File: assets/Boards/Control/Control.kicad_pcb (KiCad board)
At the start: 2 copper layers, 59.7 x 22.9 mm, 7 parts, among them J3 MAIN_BOARD, J5 MIC, SW1 SW_Push_Dual

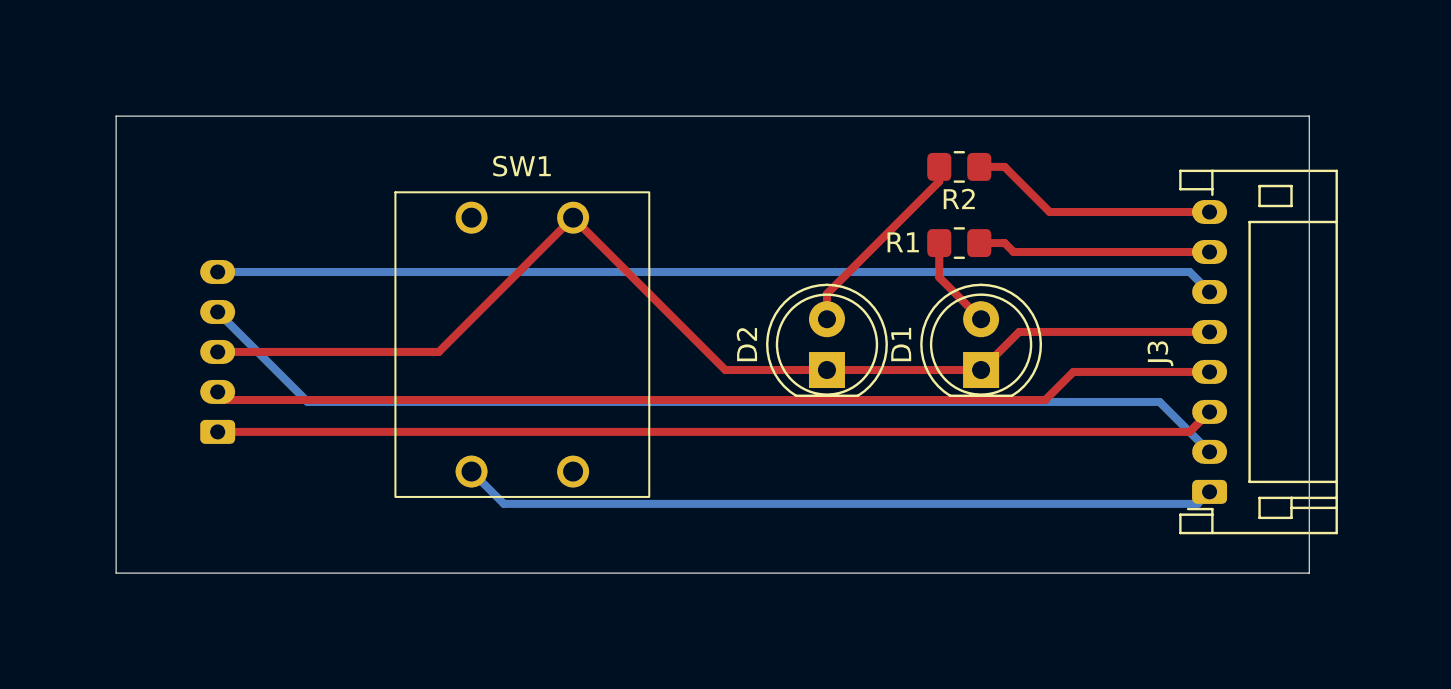
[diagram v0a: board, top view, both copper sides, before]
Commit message: Added ground plane, RF shield soldering points and text.
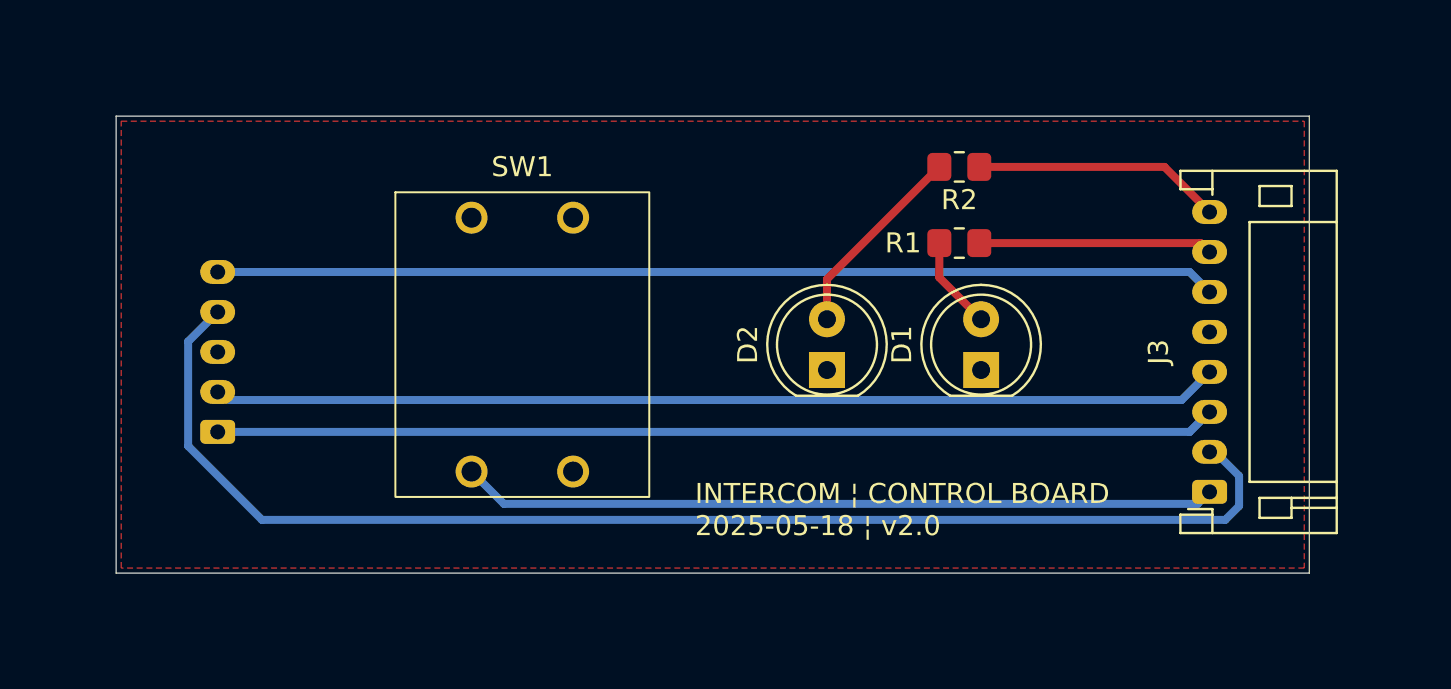
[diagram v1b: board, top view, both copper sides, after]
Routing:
- net /GND: track 56.3 -> 0.00 mm
- net Net-(J3-Pin_2): track 52.5 -> 65.2 mm
- net /3V3: track 50.4 -> 50.9 mm
- added copper zone on F.Cu, net /GND
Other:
- board text added: "INTERCOM ¦ CONTROL BOARD 2025-05-18 ¦ v2.0"
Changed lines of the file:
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@@
 		)
 		(embedded_fonts no)
-		(model "${KICAD9_3DMODEL_DIR}/Resistor_SMD.3dshapes/R_0805_2012Metric.wrl"
+		(model "${KICAD9_3DMODEL_DIR}/Resistor_SMD.3dshapes/R_0805_2012Metric.step"
 			(offset
 				(xyz 0 0 0)
@@
 		(fp_arc
 			(start -1.29 -1.54483)
-			(mid 2.071756 -2.880501)
-			(end 4.26 -0.000048)
+			(mid 2.071779 -2.880495)
+			(end 4.26 0)
 			(stroke
 				(width 0.12)
@@
 		)
 		(fp_arc
-			(start 4.26 0.000048)
-			(mid 2.071756 2.880501)
+			(start 4.26 0)
+			(mid 2.071779 2.880495)
 			(end -1.29 1.54483)
 			(stroke
@@
 		(fp_arc
 			(start -1.23 -1.469694)
-			(mid 4.17 -0.000045)
-			(end -1.229954 1.469772)
+			(mid 4.17 0)
+			(end -1.23 1.469694)
 			(stroke
 				(width 0.1)
@@
 		)
 		(embedded_fonts no)
-		(model "${KICAD9_3DMODEL_DIR}/LED_THT.3dshapes/LED_D5.0mm_Clear.wrl"
+		(model "${KICAD9_3DMODEL_DIR}/LED_THT.3dshapes/LED_D5.0mm_Clear.step"
 			(offset
 				(xyz 0 0 0)
@@
 		(fp_arc
 			(start -1.29 -1.54483)
-			(mid 2.071756 -2.880501)
-			(end 4.26 -0.000048)
+			(mid 2.071779 -2.880495)
+			(end 4.26 0)
 			(stroke
 				(width 0.12)
@@
 		)
 		(fp_arc
-			(start 4.26 0.000048)
-			(mid 2.071756 2.880501)
+			(start 4.26 0)
+			(mid 2.071779 2.880495)
 			(end -1.29 1.54483)
 			(stroke
@@
 		(fp_arc
 			(start -1.23 -1.469694)
-			(mid 4.17 -0.000045)
-			(end -1.229954 1.469772)
+			(mid 4.17 0)
+			(end -1.23 1.469694)
 			(stroke
 				(width 0.1)
@@
 		)
 		(embedded_fonts no)
-		(model "${KICAD9_3DMODEL_DIR}/LED_THT.3dshapes/LED_D5.0mm_Clear.wrl"
+		(model "${KICAD9_3DMODEL_DIR}/LED_THT.3dshapes/LED_D5.0mm_Clear.step"
 			(offset
 				(xyz 0 0 0)
@@
 		)
 		(embedded_fonts no)
-		(model "${KICAD9_3DMODEL_DIR}/Connector_JST.3dshapes/JST_PH_S8B-PH-K_1x08_P2.00mm_Horizontal.wrl"
+		(model "${KICAD9_3DMODEL_DIR}/Connector_JST.3dshapes/JST_PH_S8B-PH-K_1x08_P2.00mm_Horizontal.step"
 			(offset
 				(xyz 0 0 0)
@@
 		)
 		(embedded_fonts no)
-		(model "${KICAD9_3DMODEL_DIR}/Resistor_SMD.3dshapes/R_0805_2012Metric.wrl"
+		(model "${KICAD9_3DMODEL_DIR}/Resistor_SMD.3dshapes/R_0805_2012Metric.step"
 			(offset
 				(xyz 0 0 0)
@@
 		)
 		(embedded_fonts no)
-		(model "${KICAD9_3DMODEL_DIR}/Connector_JST.3dshapes/JST_PH_S5B-PH-K_1x05_P2.00mm_Horizontal.wrl"
+		(model "${KICAD9_3DMODEL_DIR}/Connector_JST.3dshapes/JST_PH_S5B-PH-K_1x05_P2.00mm_Horizontal.step"
 			(offset
 				(xyz 0 0 0)
@@
 		(layer "Edge.Cuts")
 	)
-	(segment
-		(start 163.92 102.87)
+	(gr_text "INTERCOM ¦ CONTROL BOARD\n2025-05-18 ¦ v2.0"
+		(at 149.606 113.792 0)
+		(layer "F.SilkS")
+		(effects
+			(font
+				(size 1 1)
+				(thickness 0.1)
+			)
+			(justify left bottom)
+		)
+	)
+	(segment
+		(start 161.83 99.06)
 		(end 161.83 100.78)
 		(width 0.4)
@@
 	(segment
 		(start 161.83 100.78)
-		(end 161.83 99.06)
+		(end 163.92 102.87)
 		(width 0.4)
 		(layer "F.Cu")
@@
 	)
 	(segment
-		(start 156.21 101.6)
-		(end 161.83 95.98)
+		(start 156.21 100.87)
+		(end 156.21 102.87)
 		(width 0.4)
 		(layer "F.Cu")
@@
 	)
 	(segment
-		(start 161.83 95.98)
-		(end 161.83 95.25)
+		(start 161.83 95.25)
+		(end 156.21 100.87)
 		(width 0.4)
 		(layer "F.Cu")
@@
 	)
 	(segment
-		(start 156.21 102.87)
-		(end 156.21 101.6)
-		(width 0.4)
-		(layer "F.Cu")
-		(net 2)
-	)
-	(segment
-		(start 125.73 102.5065)
-		(end 130.23253 107.00903)
+		(start 175.625 109.5065)
+		(end 176.826 110.7075)
 		(width 0.4)
 		(layer "B.Cu")
@@
 	)
 	(segment
-		(start 172.85253 107.00903)
-		(end 175.35 109.5065)
+		(start 175.35 109.5065)
+		(end 175.625 109.5065)
 		(width 0.4)
 		(layer "B.Cu")
@@
 	)
 	(segment
-		(start 130.23253 107.00903)
-		(end 172.85253 107.00903)
+		(start 176.134424 112.9075)
+		(end 127.945576 112.9075)
 		(width 0.4)
 		(layer "B.Cu")
@@
 	)
 	(segment
-		(start 165.1 99.06)
-		(end 165.5465 99.5065)
+		(start 176.826 110.7075)
+		(end 176.826 112.215924)
+		(width 0.4)
+		(layer "B.Cu")
+		(net 3)
+	)
+	(segment
+		(start 124.254 103.9825)
+		(end 125.73 102.5065)
+		(width 0.4)
+		(layer "B.Cu")
+		(net 3)
+	)
+	(segment
+		(start 127.945576 112.9075)
+		(end 124.254 109.215924)
+		(width 0.4)
+		(layer "B.Cu")
+		(net 3)
+	)
+	(segment
+		(start 124.254 109.215924)
+		(end 124.254 103.9825)
+		(width 0.4)
+		(layer "B.Cu")
+		(net 3)
+	)
+	(segment
+		(start 176.826 112.215924)
+		(end 176.134424 112.9075)
+		(width 0.4)
+		(layer "B.Cu")
+		(net 3)
+	)
+	(segment
+		(start 163.83 99.06)
+		(end 174.9035 99.06)
 		(width 0.4)
 		(layer "F.Cu")
@@
 	)
 	(segment
-		(start 163.83 99.06)
-		(end 165.1 99.06)
+		(start 174.9035 99.06)
+		(end 175.35 99.5065)
 		(width 0.4)
 		(layer "F.Cu")
@@
 	)
 	(segment
-		(start 165.5465 99.5065)
-		(end 175.35 99.5065)
-		(width 0.4)
-		(layer "F.Cu")
-		(net 4)
-	)
-	(segment
 		(start 125.73 100.5065)
 		(end 174.35 100.5065)
@@
 	)
 	(segment
-		(start 167.3565 97.5065)
-		(end 175.35 97.5065)
+		(start 163.83 95.25)
+		(end 173.0935 95.25)
 		(width 0.4)
 		(layer "F.Cu")
@@
 	)
 	(segment
-		(start 165.1 95.25)
-		(end 167.3565 97.5065)
+		(start 173.0935 95.25)
+		(end 175.35 97.5065)
 		(width 0.4)
 		(layer "F.Cu")
@@
 	)
 	(segment
-		(start 163.83 95.25)
-		(end 165.1 95.25)
-		(width 0.4)
-		(layer "F.Cu")
-		(net 6)
-	)
-	(segment
 		(start 174.35 108.5065)
 		(end 175.35 107.5065)
 		(width 0.4)
-		(layer "F.Cu")
+		(layer "B.Cu")
 		(net 7)
 	)
@@
 		(end 174.35 108.5065)
 		(width 0.4)
-		(layer "F.Cu")
+		(layer "B.Cu")
 		(net 7)
 	)
@@
 	)
 	(segment
-		(start 136.7935 104.5065)
-		(end 143.51 97.79)
-		(width 0.4)
-		(layer "F.Cu")
-		(net 10)
-	)
-	(segment
-		(start 151.13 105.41)
-		(end 143.51 97.79)
-		(width 0.4)
-		(layer "F.Cu")
-		(net 10)
-	)
-	(segment
-		(start 156.21 105.41)
-		(end 151.13 105.41)
-		(width 0.4)
-		(layer "F.Cu")
-		(net 10)
-	)
-	(segment
-		(start 175.35 103.5065)
-		(end 165.8235 103.5065)
-		(width 0.4)
-		(layer "F.Cu")
-		(net 10)
-	)
-	(segment
-		(start 165.8235 103.5065)
-		(end 163.92 105.41)
-		(width 0.4)
-		(layer "F.Cu")
-		(net 10)
-	)
-	(segment
-		(start 125.73 104.5065)
-		(end 136.7935 104.5065)
-		(width 0.4)
-		(layer "F.Cu")
-		(net 10)
-	)
-	(segment
-		(start 163.92 105.41)
-		(end 156.21 105.41)
-		(width 0.4)
-		(layer "F.Cu")
-		(net 10)
-	)
-	(segment
-		(start 168.54175 105.5065)
-		(end 167.13725 106.911)
+		(start 126.1345 106.911)
+		(end 125.73 106.5065)
 		(width 0.4)
 		(layer "F.Cu")
@@
 	)
 	(segment
-		(start 167.13725 106.911)
+		(start 126.1345 106.911)
+		(end 173.9455 106.911)
+		(width 0.4)
+		(layer "B.Cu")
+		(net 12)
+	)
+	(segment
+		(start 173.9455 106.911)
+		(end 175.35 105.5065)
+		(width 0.4)
+		(layer "B.Cu")
+		(net 12)
+	)
+	(segment
+		(start 125.73 106.5065)
 		(end 126.1345 106.911)
 		(width 0.4)
+		(layer "B.Cu")
+		(net 12)
+	)
+	(zone
+		(net 10)
+		(net_name "/GND")
 		(layer "F.Cu")
-		(net 12)
-	)
-	(segment
-		(start 175.35 105.5065)
-		(end 168.54175 105.5065)
-		(width 0.4)
-		(layer "F.Cu")
-		(net 12)
-	)
-	(segment
-		(start 126.1345 106.911)
-		(end 125.73 106.5065)
-		(width 0.4)
-		(layer "F.Cu")
-		(net 12)
+		(hatch edge 0.5)
+		(connect_pads
+			(clearance 0.5)
+		)
+		(min_thickness 0.25)
+		(filled_areas_thickness no)
+		(fill yes
+			(thermal_gap 0.5)
+			(thermal_bridge_width 0.5)
+		)
+		(polygon
+			(pts
+				(xy 120.904 92.964) (xy 180.086 92.964) (xy 180.086 115.316) (xy 120.904 115.316)
+			)
+		)
 	)
 	(zone

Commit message: Reworked boards.
Added LDO for the mic. Changed layout of the main board to move the cap out of the way. Added ground and power plane. Added R33's for the signal lines of the mic.
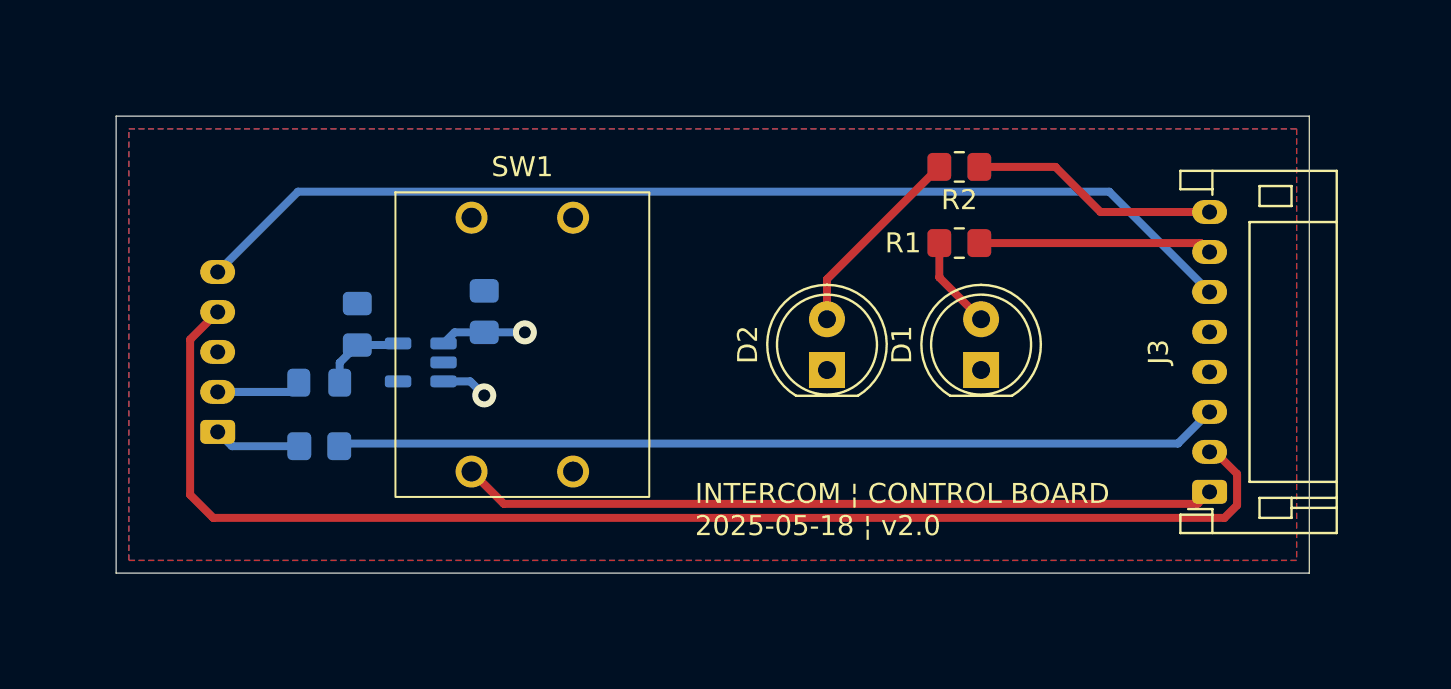
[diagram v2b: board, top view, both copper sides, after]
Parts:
- added C1: 1 0µF, Capacitor_SMD:C_0805_2012Metric_Pad1.18x1.45mm_HandSolder, B.Cu at (139.1, 102.5)
- added C2: 10 µF, Capacitor_SMD:C_0805_2012Metric_Pad1.18x1.45mm_HandSolder, B.Cu at (132.7, 103.1)
- added FB1: BLM21AG601SN1D, Inductor_SMD:L_0805_2012Metric_Pad1.15x1.40mm_HandSolder, B.Cu at (130.8, 106.0)
- added R3: 33, Resistor_SMD:R_0805_2012Metric_Pad1.20x1.40mm_HandSolder, B.Cu at (130.8, 109.2)
- added U1: TLV70033_SOT23-5, Package_TO_SOT_SMD:SOT-23-5, B.Cu at (135.9, 105.0)
- R1: value R_LED_RED -> 68
- R2: value R_LED_GREEN -> 18
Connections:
- net /GND renamed GND
- net Net-(J3-Pin_1) renamed PB
- net Net-(J3-Pin_2) renamed /MICROPHONE_WS
- net Net-(J3-Pin_6) renamed /MICROPHONE_SCK
- net Net-(J3-Pin_7) renamed LR
- net Net-(J3-Pin_8) renamed LG
- J3 pad 3: Net-(J3-Pin_3) -> /MICROPHONE_DATA
- J3 pad 4: /3V3 -> +5V
- J5 pad 1: Net-(J3-Pin_3) -> Net-(J5-Pin_1)
- J5 pad 2: /3V3 -> +3.3V
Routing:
- net /3V3: track 50.9 -> 0.00 mm
- net Net-(J3-Pin_3): track 50.0 -> 0.00 mm
- net /MICROPHONE_DATA: track 0.00 -> 44.2 mm
- net +5V: track 0.00 -> 6.63 mm, vias 0 -> 2
- net Net-(J5-Pin_1): track 0.00 -> 4.38 mm
- net /+3.3V-LDO: track 0.00 -> 4.32 mm
- net +3.3V: track 0.00 -> 4.25 mm
- net /MICROPHONE_SCK: track 50.0 -> 54.1 mm
- net /MICROPHONE_WS: track 65.2 -> 66.7 mm
- added copper zone on F.Cu, net +5V
- added copper zone on B.Cu, net GND
- removed copper zone on F.Cu, net GND

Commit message: Fixed ERC errors. Switched to double ground plane instead of ground and power plane. Switched to 1uF caps for the LDO conforming to the data sheet. Added logo.
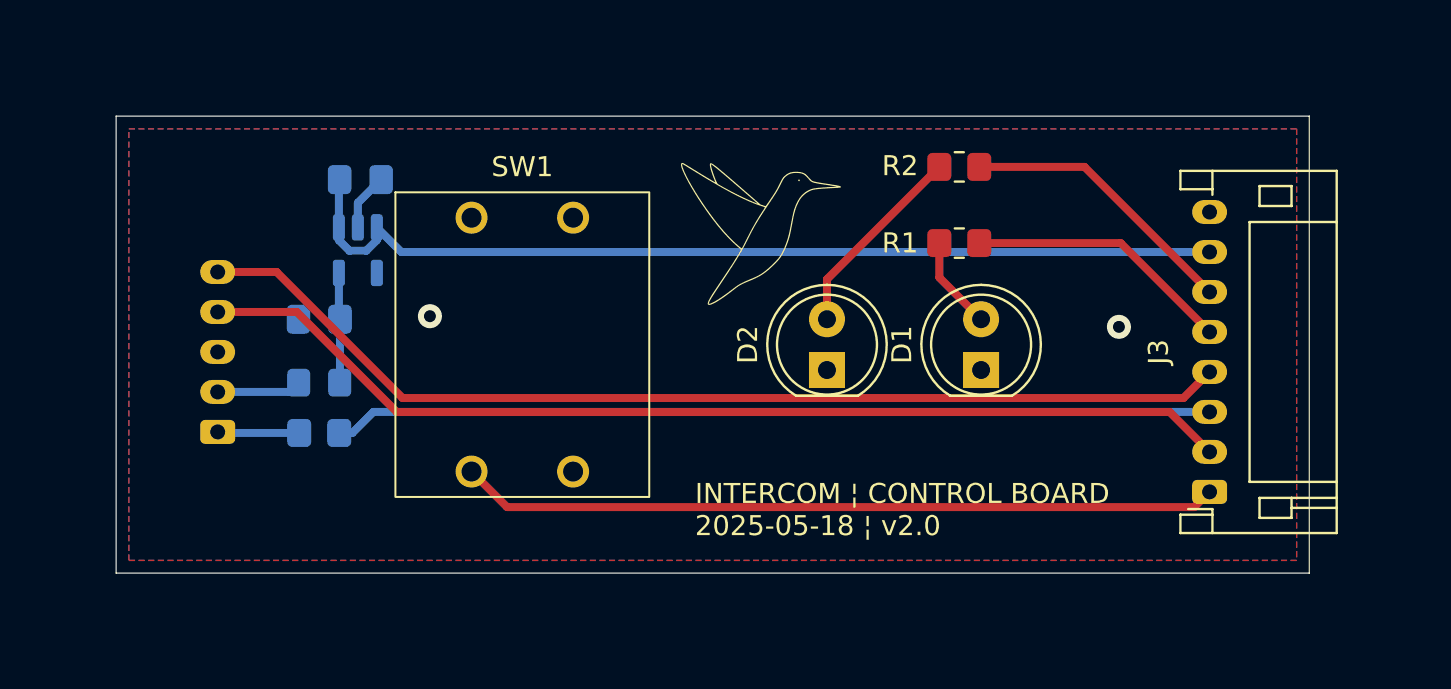
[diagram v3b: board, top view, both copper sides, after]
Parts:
- added G***: LOGO, Custom Footprints:Eletronica Logo, F.Cu at (152.9, 98.6)
- C1: value 1 0µF -> 1µF
- C2: value 10 µF -> 1µF
- moved C1 9.06 mm to (132.9, 95.9), turned to 180 degrees
- moved U1 6.44 mm to (132.7, 99.4), turned to -90 degrees
- moved C2 1.92 mm to (130.8, 102.9), turned to 180 degrees
- moved R3 0.66 mm to (130.8, 108.6)
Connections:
- J3 pad 4: +5V -> /MICROPHONE_SCK
- J3 pad 5: GND -> LR
- J3 pad 6: /MICROPHONE_SCK -> LG
- J3 pad 7: LR -> +5V
- J3 pad 8: LG -> GND
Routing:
- net +5V: track 6.63 -> 48.2 mm, vias 2 -> 0
- net /MICROPHONE_WS: track 66.7 -> 52.5 mm
- net GND: track 0.00 -> 2.87 mm, vias 0 -> 2
- net LG: track 12.5 -> 14.1 mm
- net LR: track 11.7 -> 13.4 mm
- net /MICROPHONE_SCK: track 54.1 -> 52.8 mm
- net /+3.3V-LDO: track 4.32 -> 5.52 mm
- added copper zone on F.Cu, net GND
- removed copper zone on F.Cu, net +5V

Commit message: Applied suggestions from Rick Hartley.
See https://www.youtube.com/watch?v=ySuUZEjARPY.
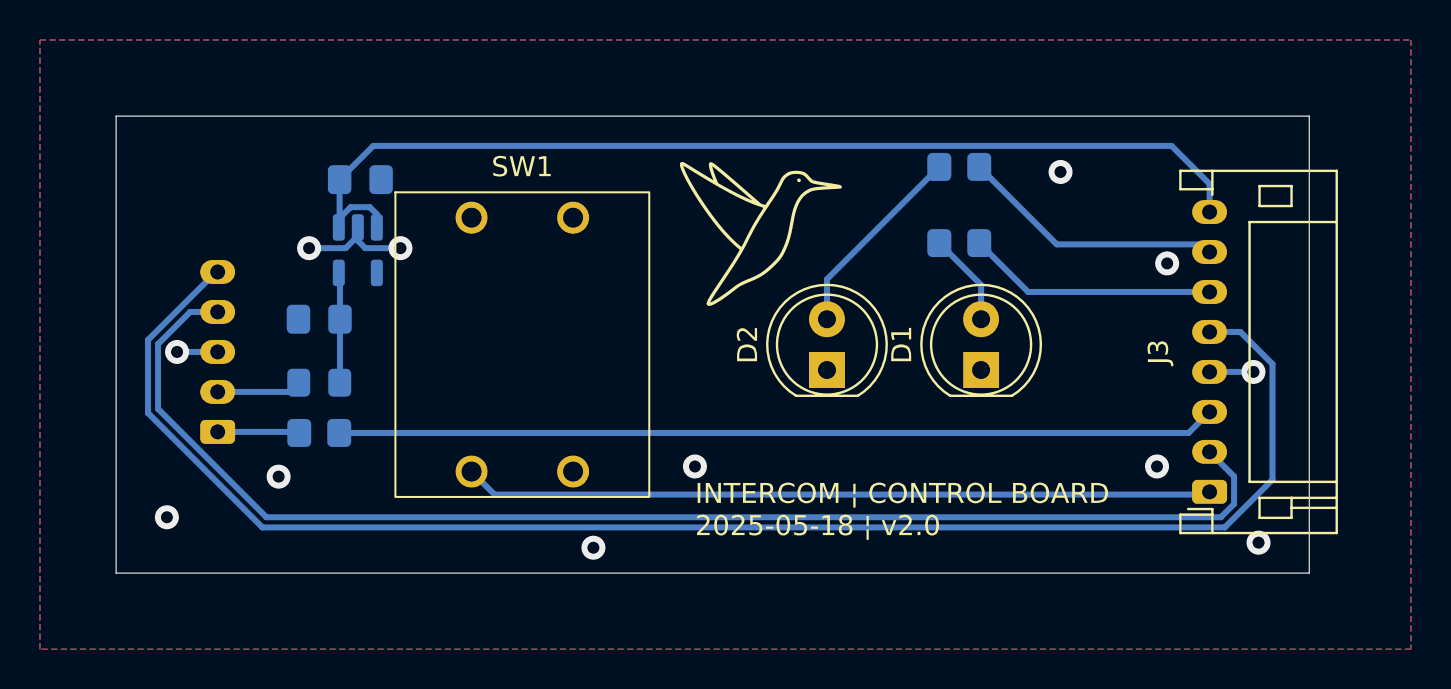
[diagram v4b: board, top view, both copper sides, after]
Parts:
- R1, R2: moved to B.Cu
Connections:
- J3 pad 4: /MICROPHONE_SCK -> GND
- J3 pad 5: LR -> /MICROPHONE_SCK
- J3 pad 6: LG -> LR
- J3 pad 7: +5V -> LG
- J3 pad 8: GND -> +5V
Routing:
- net /MICROPHONE_SCK: track 52.8 -> 77.8 mm
- net /MICROPHONE_WS: track 52.5 -> 66.4 mm
- net GND: track 2.87 -> 10.3 mm, vias 2 -> 12
- net +5V: track 48.2 -> 52.2 mm
- net LR: track 13.4 -> 12.5 mm
- net LG: track 14.1 -> 13.3 mm
- net PB: track 38.1 -> 37.5 mm
